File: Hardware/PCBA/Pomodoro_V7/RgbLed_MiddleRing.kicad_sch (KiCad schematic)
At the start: 16 parts

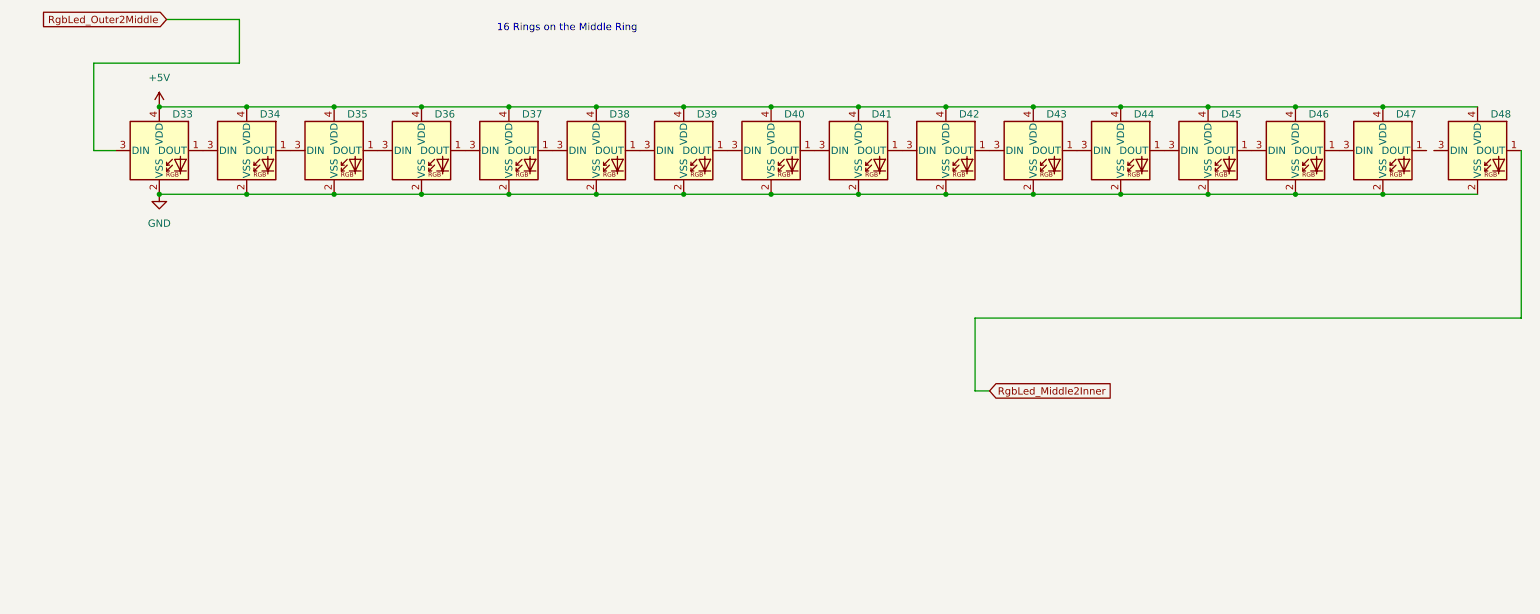
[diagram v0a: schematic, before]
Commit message: FW can now be flashed to an ESP32-S2 Target; Completed the Schematic
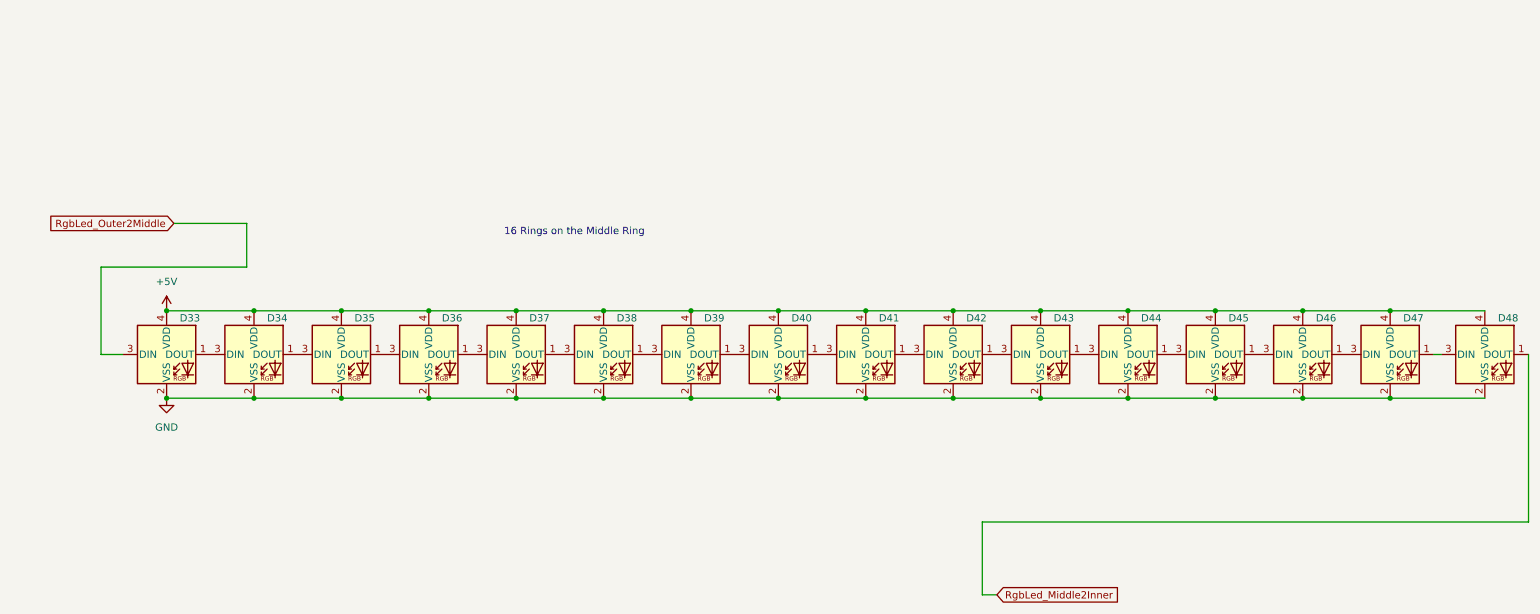
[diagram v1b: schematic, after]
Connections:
- net at D48.3 (DIN): now also D47.1 (DOUT)
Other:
- moved on the sheet: D33, D34, D35, D36, D37, D38, D39, D40, D41, D42, D43, D44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
